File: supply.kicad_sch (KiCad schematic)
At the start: 110 parts, among them J1 USB4105-GF-A, Q1 2N7002, Q2 BCM857BS-7-F, Q3 AO3401A, U1 MP20073, U10 AP7330-W5-7, U2 LM339, U3 LM339, U4 DIO7553ST6, U5 AP62301WU-7, U6 AP62301WU-7, U7 AP62301WU-7, U8 AP7330-W5-7, U9 AP7330-W5-7

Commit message: Completed the layout of the PSU
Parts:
- removed R29, R30, R37: R_0R_0402, crosslink-nx-video-converter-footprints:0402-res, symbol crosslink-nx-video-converter:R_0R_0402
- added R29, R30, R37: R_0R_0603, antmicro-footprints:0603-res, symbol antmicroResistors0603:R_0R_0603
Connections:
- net +1V2: now also R30.2
- net +1V8: now also R37.2
- net 1V0_Clean: now also R29.2
- net at R31.2, U8.5 (Vout): now also R29.1
- net FFC2_5V_1: now reaches C4.1, R4.2, R6.2, R63.2, U4.1 (IN)
- net 5V_I: now reaches Q2.1, Q3.2 (S), R13.1, U4.6 (OUT)
- net at R33.2, U9.5 (Vout): now also R30.1
- net at R35.2, U10.5 (Vout): now also R37.1
- net 1V0_IN renamed 5V_1V0_IN
- net 1V5_IN renamed 5V_1V5_IN
- net 3V3_IN renamed 5V_3V3_IN
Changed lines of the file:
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@@
     (effects (font (size 1.27 1.27)) (justify left bottom))
   )
-  (label "1V0_IN" (at 267.97 71.755 0)
+  (label "5V_1V0_IN" (at 274.32 71.755 0)
     (effects (font (size 1.27 1.27)) (justify left bottom))
   )
@@
     (effects (font (size 1.27 1.27)) (justify left bottom))
   )
-  (label "3V3_IN" (at 269.24 39.37 0)
+  (label "5V_3V3_IN" (at 274.32 39.37 0)
     (effects (font (size 1.27 1.27)) (justify left bottom))
   )
@@
     (effects (font (size 1.27 1.27)) (justify left bottom))
   )
+  (label "FFC2_5V_1" (at 49.53 77.47 0)
+    (effects (font (size 1.27 1.27)) (justify left bottom))
+  )
   (label "VREF_0V45" (at 50.8 273.05 0)
     (effects (font (size 1.27 1.27)) (justify left bottom))
@@
     (effects (font (size 1.27 1.27)) (justify left bottom))
   )
-  (label "1V5_IN" (at 267.97 105.41 0)
+  (label "5V_1V5_IN" (at 274.955 105.41 0)
+    (effects (font (size 1.27 1.27)) (justify left bottom))
+  )
+  (label "5V_I" (at 105.41 77.47 0)
     (effects (font (size 1.27 1.27)) (justify left bottom))
   )
@@
     (pin "3")
   )
+  (symbol (lib_id "antmicroResistors0603:R_0R_0603") (at 351.79 222.25 0) (unit 1)
+    (in_bom yes) (on_board yes)
+    (property "Reference" "R37" (id 0) (at 351.79 219.71 0)
+      (effects (font (size 1.524 1.524)))
+    )
+    (property "Value" "R_0R_0603" (id 1) (at 351.79 226.06 0)
+      (effects (font (size 1.524 1.524)) hide)
+    )
+    (property "Footprint" "antmicro-footprints:0603-res" (id 2) (at 356.87 217.17 0)
+      (effects (font (size 1.524 1.524)) (justify left) hide)
+    )
+    (property "Datasheet" "" (id 3) (at 351.79 222.25 0)
+      (effects (font (size 1.27 1.27)) hide)
+    )
+    (property "Manufacturer" "BOURNS" (id 4) (at 356.87 212.09 0)
+      (effects (font (size 1.524 1.524)) (justify left) hide)
+    )
+    (property "MPN" "CR0603-J/-000ELF" (id 5) (at 356.87 214.63 0)
+      (effects (font (size 1.524 1.524)) (justify left) hide)
+    )
+    (property "Val" "0R" (id 6) (at 351.79 222.25 0))
+    (pin "1")
+    (pin "2")
+  )
   (symbol (lib_id "crosslink-nx-video-converter:GND") (at 345.44 210.82 0) (unit 1)
     (in_bom yes) (on_board yes)
@@
     (pin "2")
   )
-  (symbol (lib_id "crosslink-nx-video-converter:R_0R_0402") (at 351.79 191.77 0) (unit 1)
-    (in_bom yes) (on_board yes)
-    (property "Reference" "R30" (id 0) (at 350.393 188.341 0)
-      (effects (font (size 1.524 1.524)) (justify left))
-    )
-    (property "Value" "R_0R_0402" (id 1) (at 351.79 195.58 0)
-      (effects (font (size 1.524 1.524)) hide)
-    )
-    (property "Footprint" "crosslink-nx-video-converter-footprints:0402-res" (id 2) (at 356.87 186.69 0)
-      (effects (font (size 1.524 1.524)) (justify left) hide)
-    )
-    (property "Datasheet" "" (id 3) (at 351.79 191.77 0)
-      (effects (font (size 1.27 1.27)) hide)
-    )
-    (property "Manufacturer" "PANASONIC" (id 4) (at 356.87 181.61 0)
-      (effects (font (size 1.524 1.524)) (justify left) hide)
-    )
-    (property "MPN" "ERJ2GE0R00X" (id 5) (at 356.87 184.15 0)
-      (effects (font (size 1.524 1.524)) (justify left) hide)
-    )
-    (property "Val" "0R" (id 6) (at 351.79 194.31 0))
-    (pin "1")
-    (pin "2")
-  )
   (symbol (lib_id "crosslink-nx-video-converter:R_10k_0402") (at 113.03 186.69 90) (unit 1)
     (in_bom yes) (on_board yes) (fields_autoplaced)
@@
     (pin "3")
   )
-  (symbol (lib_id "crosslink-nx-video-converter:R_0R_0402") (at 351.79 161.29 0) (unit 1)
-    (in_bom yes) (on_board yes)
-    (property "Reference" "R29" (id 0) (at 350.393 157.861 0)
-      (effects (font (size 1.524 1.524)) (justify left))
-    )
-    (property "Value" "R_0R_0402" (id 1) (at 351.79 165.1 0)
-      (effects (font (size 1.524 1.524)) hide)
-    )
-    (property "Footprint" "crosslink-nx-video-converter-footprints:0402-res" (id 2) (at 356.87 156.21 0)
-      (effects (font (size 1.524 1.524)) (justify left) hide)
-    )
-    (property "Datasheet" "" (id 3) (at 351.79 161.29 0)
-      (effects (font (size 1.27 1.27)) hide)
-    )
-    (property "Manufacturer" "PANASONIC" (id 4) (at 356.87 151.13 0)
-      (effects (font (size 1.524 1.524)) (justify left) hide)
-    )
-    (property "MPN" "ERJ2GE0R00X" (id 5) (at 356.87 153.67 0)
-      (effects (font (size 1.524 1.524)) (justify left) hide)
-    )
-    (property "Val" "0R" (id 6) (at 351.79 163.83 0))
-    (pin "1")
-    (pin "2")
-  )
   (symbol (lib_id "crosslink-nx-video-converter:GND") (at 64.77 130.81 0) (unit 1)
     (in_bom yes) (on_board yes)
@@
   (symbol (lib_id "crosslink-nx-video-converter:TP_SMD_0_75MM") (at 48.26 91.44 0) (unit 1)
     (in_bom yes) (on_board yes)
-    (property "Reference" "TP23" (id 0) (at 52.07 90.17 0)
+    (property "Reference" "TP23" (id 0) (at 53.34 90.17 0)
       (effects (font (size 1.27 1.27)) (justify right))
     )
@@
     (pin "1")
   )
+  (symbol (lib_id "antmicroResistors0603:R_0R_0603") (at 351.79 191.77 0) (unit 1)
+    (in_bom yes) (on_board yes)
+    (property "Reference" "R30" (id 0) (at 351.79 189.23 0)
+      (effects (font (size 1.524 1.524)))
+    )
+    (property "Value" "R_0R_0603" (id 1) (at 351.79 195.58 0)
+      (effects (font (size 1.524 1.524)) hide)
+    )
+    (property "Footprint" "antmicro-footprints:0603-res" (id 2) (at 356.87 186.69 0)
+      (effects (font (size 1.524 1.524)) (justify left) hide)
+    )
+    (property "Datasheet" "" (id 3) (at 351.79 191.77 0)
+      (effects (font (size 1.27 1.27)) hide)
+    )
+    (property "Manufacturer" "BOURNS" (id 4) (at 356.87 181.61 0)
+      (effects (font (size 1.524 1.524)) (justify left) hide)
+    )
+    (property "MPN" "CR0603-J/-000ELF" (id 5) (at 356.87 184.15 0)
+      (effects (font (size 1.524 1.524)) (justify left) hide)
+    )
+    (property "Val" "0R" (id 6) (at 351.79 191.77 0))
+    (pin "1")
+    (pin "2")
+  )
   (symbol (lib_id "crosslink-nx-video-converter:GND") (at 68.58 44.45 0) (unit 1)
     (in_bom yes) (on_board yes)
@@
     (pin "6")
   )
-  (symbol (lib_id "crosslink-nx-video-converter:R_0R_0402") (at 351.79 222.25 0) (unit 1)
-    (in_bom yes) (on_board yes)
-    (property "Reference" "R37" (id 0) (at 350.393 218.821 0)
-      (effects (font (size 1.524 1.524)) (justify left))
-    )
-    (property "Value" "R_0R_0402" (id 1) (at 351.79 226.06 0)
-      (effects (font (size 1.524 1.524)) hide)
-    )
-    (property "Footprint" "crosslink-nx-video-converter-footprints:0402-res" (id 2) (at 356.87 217.17 0)
-      (effects (font (size 1.524 1.524)) (justify left) hide)
-    )
-    (property "Datasheet" "" (id 3) (at 351.79 222.25 0)
-      (effects (font (size 1.27 1.27)) hide)
-    )
-    (property "Manufacturer" "PANASONIC" (id 4) (at 356.87 212.09 0)
-      (effects (font (size 1.524 1.524)) (justify left) hide)
-    )
-    (property "MPN" "ERJ2GE0R00X" (id 5) (at 356.87 214.63 0)
-      (effects (font (size 1.524 1.524)) (justify left) hide)
-    )
-    (property "Val" "0R" (id 6) (at 351.79 224.79 0))
-    (pin "1")
-    (pin "2")
-  )
   (symbol (lib_id "crosslink-nx-video-converter:R_10k_0402") (at 335.28 86.995 90) (unit 1)
     (in_bom yes) (on_board yes)
@@
     (pin "S1")
   )
+  (symbol (lib_id "antmicroResistors0603:R_0R_0603") (at 351.79 161.29 0) (unit 1)
+    (in_bom yes) (on_board yes)
+    (property "Reference" "R29" (id 0) (at 351.79 158.75 0)
+      (effects (font (size 1.524 1.524)))
+    )
+    (property "Value" "R_0R_0603" (id 1) (at 351.79 165.1 0)
+      (effects (font (size 1.524 1.524)) hide)
+    )
+    (property "Footprint" "antmicro-footprints:0603-res" (id 2) (at 356.87 156.21 0)
+      (effects (font (size 1.524 1.524)) (justify left) hide)
+    )
+    (property "Datasheet" "" (id 3) (at 351.79 161.29 0)
+      (effects (font (size 1.27 1.27)) hide)
+    )
+    (property "Manufacturer" "BOURNS" (id 4) (at 356.87 151.13 0)
+      (effects (font (size 1.524 1.524)) (justify left) hide)
+    )
+    (property "MPN" "CR0603-J/-000ELF" (id 5) (at 356.87 153.67 0)
+      (effects (font (size 1.524 1.524)) (justify left) hide)
+    )
+    (property "Val" "0R" (id 6) (at 351.79 161.29 0))
+    (pin "1")
+    (pin "2")
+  )
   (symbol (lib_id "crosslink-nx-video-converter:R_0R_0805") (at 262.89 71.755 0) (unit 1)

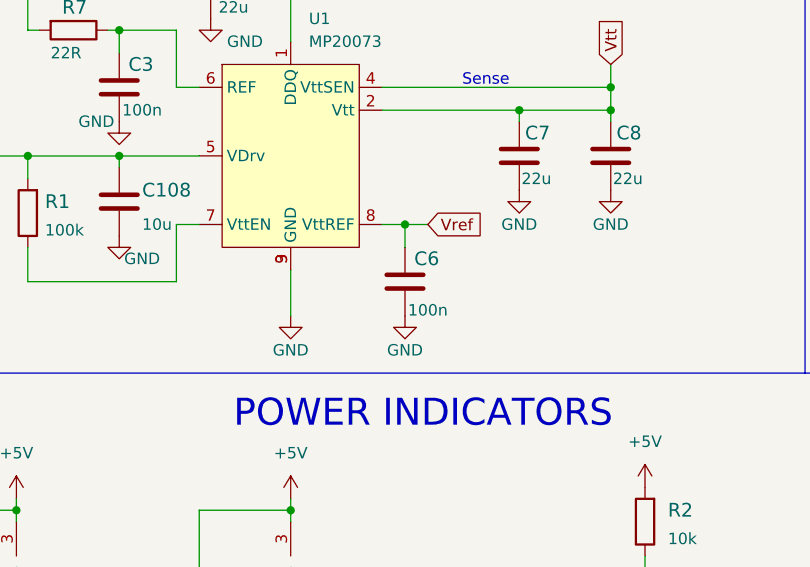
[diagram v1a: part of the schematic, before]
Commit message: Routed rest of low speed signals
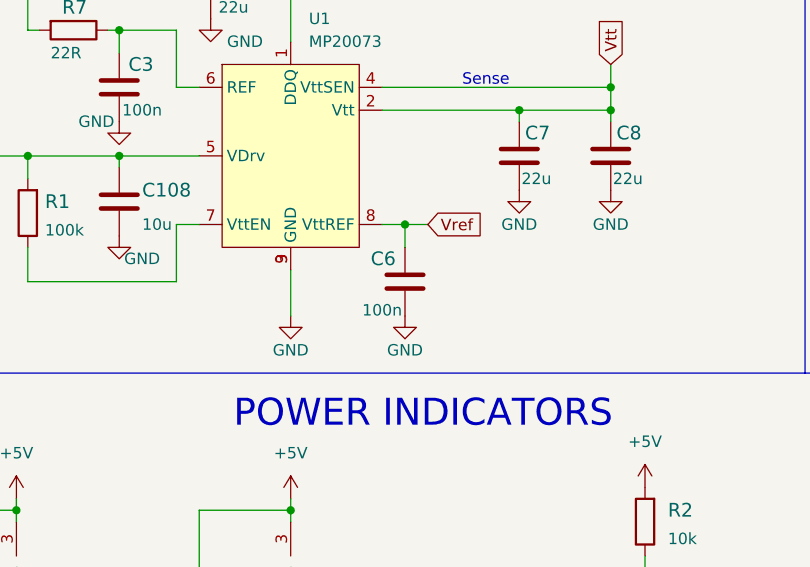
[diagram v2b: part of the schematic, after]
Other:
- moved on the sheet: C6
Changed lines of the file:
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@@
     (pin "1")
   )
-  (symbol (lib_id "crosslink-nx-video-converter:C_100n_0402") (at 86.36 160.02 180) (unit 1)
+  (symbol (lib_id "crosslink-nx-video-converter:C_100n_0402") (at 86.36 160.02 0) (mirror x) (unit 1)
     (in_bom yes) (on_board yes)
-    (property "Reference" "C6" (id 0) (at 90.17 157.48 0)
+    (property "Reference" "C6" (id 0) (at 82.55 157.48 0)
       (effects (font (size 1.524 1.524)) (justify left))
     )
@@
       (effects (font (size 1.524 1.524)) hide)
     )
-    (property "Footprint" "crosslink-nx-video-converter-footprints:0402-cap" (id 2) (at 81.28 165.1 0)
+    (property "Footprint" "crosslink-nx-video-converter-footprints:0402-cap" (id 2) (at 91.44 165.1 0)
       (effects (font (size 1.524 1.524)) (justify left) hide)
     )
@@
       (effects (font (size 1.27 1.27)) hide)
     )
-    (property "Manufacturer" "Murata" (id 4) (at 81.28 170.18 0)
+    (property "Manufacturer" "Murata" (id 4) (at 91.44 170.18 0)
       (effects (font (size 1.524 1.524)) (justify left) hide)
     )
-    (property "MPN" "GRM155R61H104KE14D" (id 5) (at 81.28 167.64 0)
+    (property "MPN" "GRM155R61H104KE14D" (id 5) (at 91.44 167.64 0)
       (effects (font (size 1.524 1.524)) (justify left) hide)
     )
-    (property "Val" "100n" (id 6) (at 88.9 163.195 0))
+    (property "Val" "100n" (id 6) (at 83.82 163.195 0))
     (pin "1")
     (pin "2")

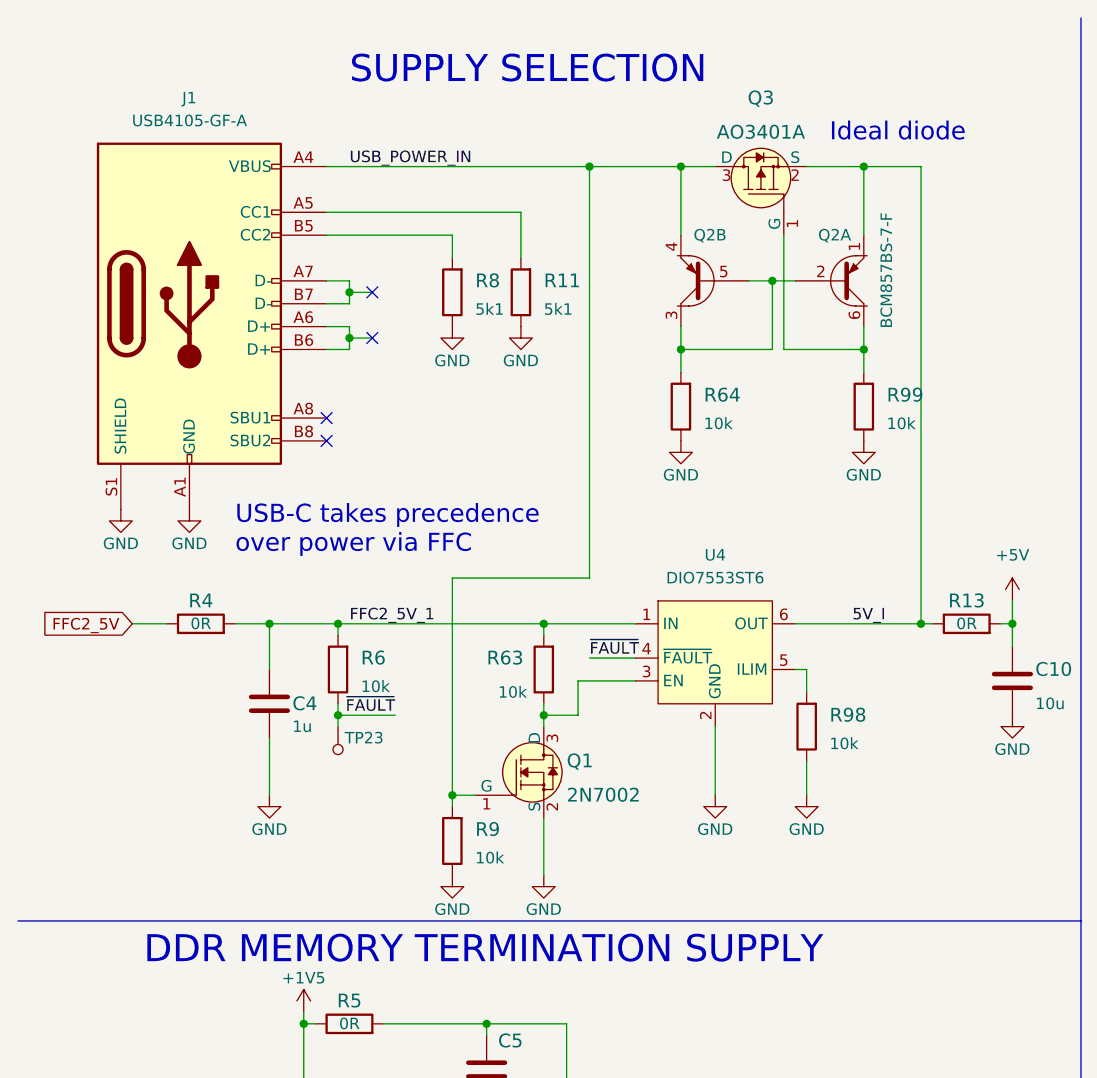
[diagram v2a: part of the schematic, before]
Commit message: Added FT230XQ-R for USB connectivity
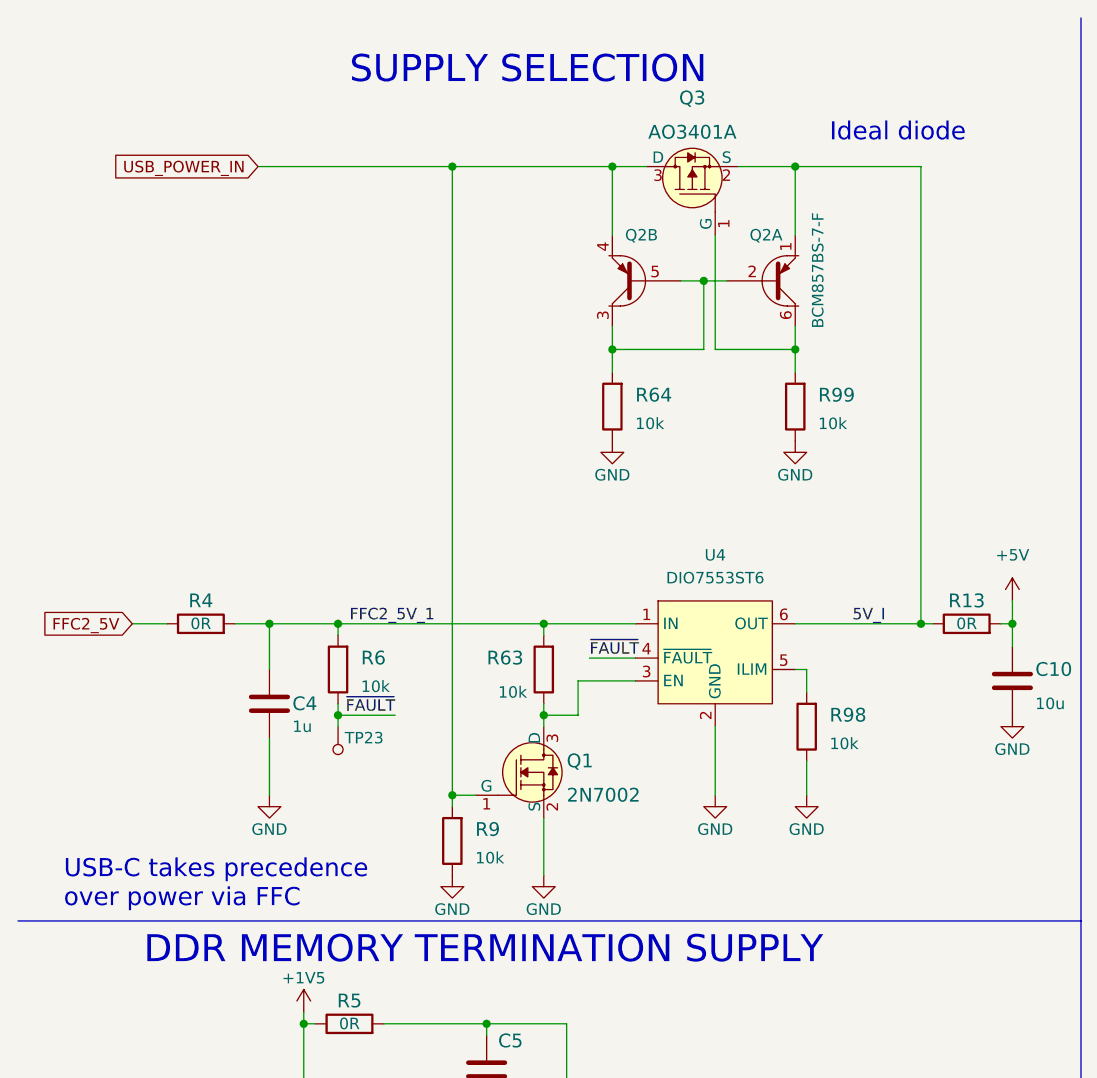
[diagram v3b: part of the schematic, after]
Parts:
- removed J1: USB4105-GF-A, antmicro-footprints:GCT_USB4105-GF-A, symbol antmicroUSBDVIHDMIConnectors:USB4105-GF-A
- removed R11, R8: R_5k1_0402, antmicro-footprints:0402-res, symbol antmicroResistors0402:R_5k1_0402
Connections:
- no-connect marks 5 -> 1
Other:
- moved on the sheet: Q2A, Q2B, Q3, R64, R99

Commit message: Created loclib
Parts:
- Q1: footprint antmicro-footprints:SOT-23-3 -> crosslink-nx-video-converter-footprints:SOT-23-3; symbol antmicroTransistorsFETsMOSFETsSingle:2N7002 -> crosslink-nx-video-converter:2N7002
- Q2: footprint antmicro-footprints:SOT-363 -> crosslink-nx-video-converter-footprints:SOT-363; symbol antmicroTransistorsBipolarArrays:BCM857BS-7-F -> crosslink-nx-video-converter:BCM857BS-7-F
- Q3: footprint antmicro-footprints:SOT-23-3 -> crosslink-nx-video-converter-footprints:SOT-23-3; symbol antmicroTransistorsFETsMOSFETsSingle:AO3401A -> crosslink-nx-video-converter:AO3401A
- R13, R4: footprint antmicro-footprints:1206-res -> crosslink-nx-video-converter-footprints:1206-res; symbol antmicroResistorsmisc:R_0R_1206 -> crosslink-nx-video-converter:R_0R_1206
- R29, R30, R37: footprint antmicro-footprints:0603-res -> crosslink-nx-video-converter-footprints:0603-res; symbol antmicroResistors0603:R_0R_0603 -> crosslink-nx-video-converter:R_0R_0603
- U1: footprint antmicro-footprints:MSOP-8-1EP_W3mm -> crosslink-nx-video-converter-footprints:MSOP-8-1EP_W3mm; symbol antmicroPMICVoltageRegulatorsLinear:MP20073 -> crosslink-nx-video-converter:MP20073
- U4: footprint antmicro-footprints:SOT23-6L -> crosslink-nx-video-converter-footprints:SOT23-6L; symbol antmicroPMICPowerDistributionSwitchesLoadDrivers:DIO7553ST6 -> crosslink-nx-video-converter:DIO7553ST6

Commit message: Added revision and title to the schematic sheets
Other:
- title: (none) -> CrossLink-NX Video Converter
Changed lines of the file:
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@@
 (kicad_sch (version 20211123) (generator eeschema)
   (paper "A3")
+  (title_block
+    (title "CrossLink-NX Video Converter")
+    (date "2022-10-27")
+    (rev "1.0.0")
+    (comment 1 "www.antmicro.com")
+    (comment 2 "Antmicro Ltd.")
+  )
   (junction (at 43.18 204.47) (diameter 0) (color 0 0 0 0)
   )
